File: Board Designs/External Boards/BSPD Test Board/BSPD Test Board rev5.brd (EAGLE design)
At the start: 64 x 85.8 mm, 30 parts

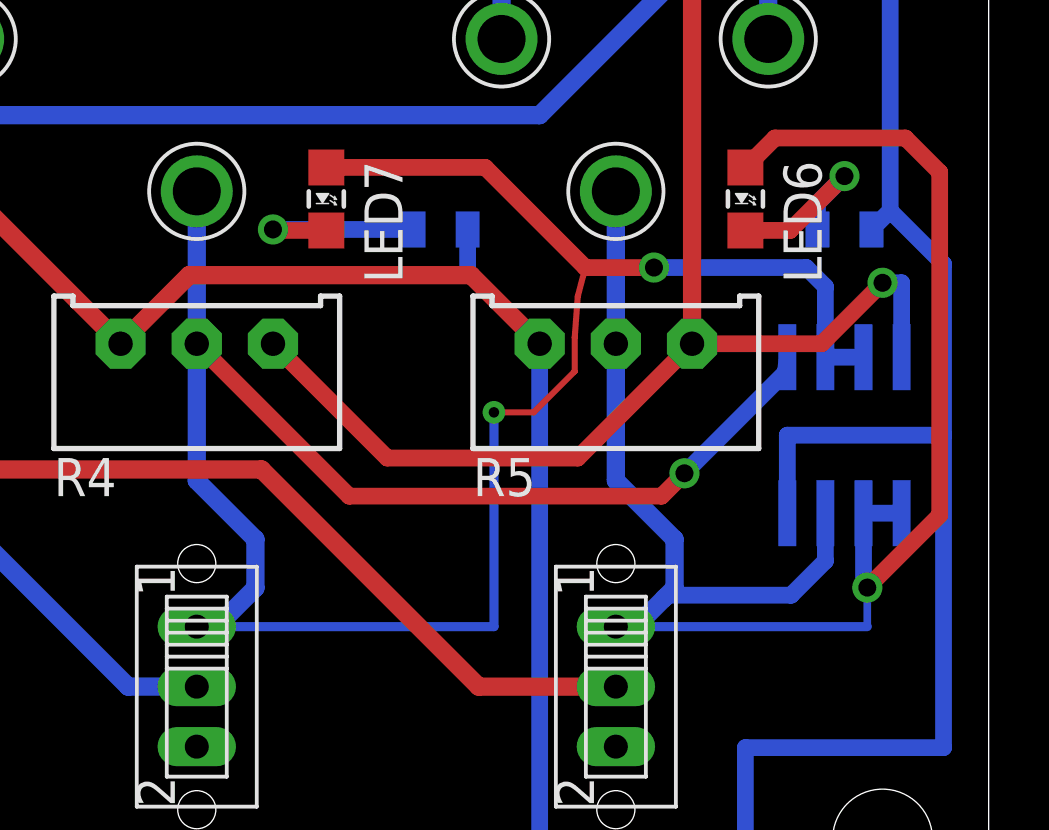
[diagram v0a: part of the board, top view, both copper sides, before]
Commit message: Minor routing changes
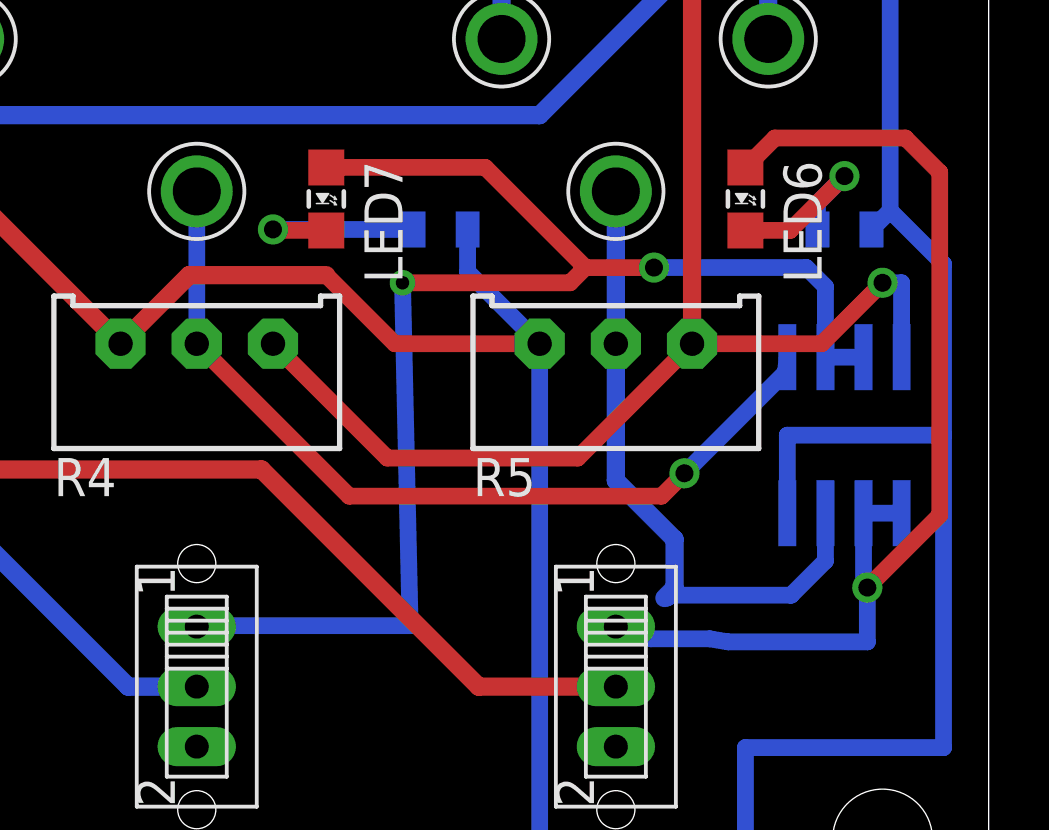
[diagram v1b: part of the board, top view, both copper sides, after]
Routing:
- net N$4: track 40.3 -> 29.0 mm, vias 2 -> 1
- net N$5: track 23.8 -> 22.0 mm
- net N$9: track 45.7 -> 46.8 mm
- net N$8: track 35.8 -> 36.3 mm
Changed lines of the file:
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@@
 </class>
 </classes>
-<designrules name="default">
+<designrules name="DRC Advanced Circuits">
 <description language="de">&lt;b&gt;EAGLE Design Rules&lt;/b&gt;
 &lt;p&gt;
@@
 <param name="mtCopper" value="0.035mm 0.035mm 0.035mm 0.035mm 0.035mm 0.035mm 0.035mm 0.035mm 0.035mm 0.035mm 0.035mm 0.035mm 0.035mm 0.035mm 0.035mm 0.035mm"/>
 <param name="mtIsolate" value="1.5mm 0.15mm 0.2mm 0.15mm 0.2mm 0.15mm 0.2mm 0.15mm 0.2mm 0.15mm 0.2mm 0.15mm 0.2mm 0.15mm 0.2mm"/>
-<param name="mdWireWire" value="8mil"/>
-<param name="mdWirePad" value="8mil"/>
-<param name="mdWireVia" value="8mil"/>
-<param name="mdPadPad" value="8mil"/>
-<param name="mdPadVia" value="8mil"/>
-<param name="mdViaVia" value="8mil"/>
-<param name="mdSmdPad" value="8mil"/>
-<param name="mdSmdVia" value="8mil"/>
-<param name="mdSmdSmd" value="8mil"/>
-<param name="mdViaViaSameLayer" value="8mil"/>
+<param name="mdWireWire" value="6mil"/>
+<param name="mdWirePad" value="6mil"/>
+<param name="mdWireVia" value="6mil"/>
+<param name="mdPadPad" value="6mil"/>
+<param name="mdPadVia" value="6mil"/>
+<param name="mdViaVia" value="6mil"/>
+<param name="mdSmdPad" value="6mil"/>
+<param name="mdSmdVia" value="6mil"/>
+<param name="mdSmdSmd" value="6mil"/>
+<param name="mdViaViaSameLayer" value="6mil"/>
 <param name="mnLayersViaInSmd" value="2"/>
 <param name="mdCopperDimension" value="40mil"/>
-<param name="mdDrill" value="8mil"/>
+<param name="mdDrill" value="6mil"/>
 <param name="mdSmdStop" value="0mil"/>
-<param name="msWidth" value="10mil"/>
-<param name="msDrill" value="24mil"/>
+<param name="msWidth" value="6mil"/>
+<param name="msDrill" value="15mil"/>
 <param name="msMicroVia" value="9.99mm"/>
 <param name="msBlindViaRatio" value="0.5"/>
@@
 <wire x1="23.368" y1="63.754" x2="20.422" y2="63.754" width="0.6096" layer="16"/>
 <wire x1="35.052" y1="20.32" x2="37.338" y2="22.606" width="0.6096" layer="1"/>
-<wire x1="46.736" y1="22.606" x2="49.022" y2="20.32" width="0.6096" layer="1"/>
-<wire x1="37.338" y1="22.606" x2="46.736" y2="22.606" width="0.6096" layer="1"/>
+<wire x1="41.91" y1="22.606" x2="37.338" y2="22.606" width="0.6096" layer="1"/>
 <contactref element="U$7" pad="4"/>
 <contactref element="R9" pad="2"/>
@@
 <wire x1="2.794" y1="22.86" x2="5.886" y2="22.86" width="0.5588" layer="16"/>
 <wire x1="49.022" y1="20.32" x2="49.022" y2="2.59926875" width="0.5588" layer="16"/>
-<wire x1="62.484" y1="6.5659" x2="62.484" y2="6.858" width="0" layer="19" extent="1-16"/>
 <wire x1="62.484" y1="6.858" x2="62.484" y2="17.272" width="0.5588" layer="16"/>
 <wire x1="49.022" y1="2.59926875" x2="55.88" y2="2.59926875" width="0.5588" layer="16"/>
 <wire x1="55.88" y1="2.59926875" x2="55.88" y2="6.858" width="0.5588" layer="16"/>
 <wire x1="55.88" y1="6.858" x2="62.484" y2="6.858" width="0.5588" layer="16"/>
+<wire x1="49.022" y1="20.32" x2="44.196" y2="20.32" width="0.5588" layer="1"/>
+<wire x1="44.196" y1="20.32" x2="41.91" y2="22.606" width="0.5588" layer="1"/>
 </signal>
 <signal name="N$1">
@@
 <contactref element="R4" pad="2"/>
 <contactref element="U$2" pad="P$1"/>
-<wire x1="37.592" y1="20.32" x2="37.592" y2="25.4" width="0.6096" layer="16"/>
-<wire x1="38.402125" y1="11.0363" x2="39.5478" y2="12.181975" width="0.6096" layer="16"/>
-<wire x1="39.5478" y1="12.181975" x2="39.5478" y2="13.802225" width="0.6096" layer="16"/>
-<wire x1="37.7383" y1="11.0363" x2="38.402125" y2="11.0363" width="0.6096" layer="16"/>
-<wire x1="37.592" y1="15.758025" x2="37.592" y2="20.32" width="0.6096" layer="16"/>
-<wire x1="39.5478" y1="13.802225" x2="37.592" y2="15.758025" width="0.6096" layer="16"/>
 <contactref element="U$7" pad="5"/>
 <wire x1="57.277" y1="19.872" x2="57.21" y2="19.364" width="0.5588" layer="16"/>
@@
 <wire x1="42.672" y1="15.24" x2="37.592" y2="20.32" width="0.5588" layer="1"/>
 <wire x1="53.086" y1="15.24" x2="42.672" y2="15.24" width="0.5588" layer="1"/>
-<via x="37.592" y="25.4" extent="1-16" drill="0.35"/>
+<wire x1="37.592" y1="25.4" x2="37.592" y2="20.32" width="0.5588" layer="16"/>
 </signal>
 <signal name="N$5">
@@
 <contactref element="U$3" pad="P$1"/>
 <wire x1="51.562" y1="20.32" x2="51.562" y2="25.4" width="0.6096" layer="16"/>
-<wire x1="53.1799125" y1="11.8440875" x2="52.372125" y2="11.0363" width="0.6096" layer="16"/>
 <wire x1="53.1799125" y1="11.8440875" x2="53.5178" y2="12.181975" width="0.6096" layer="16"/>
 <wire x1="53.5178" y1="12.181975" x2="53.5178" y2="13.802225" width="0.6096" layer="16"/>
-<wire x1="51.7083" y1="11.0363" x2="52.372125" y2="11.0363" width="0.6096" layer="16"/>
 <wire x1="51.562" y1="15.758025" x2="51.562" y2="20.32" width="0.6096" layer="16"/>
 <wire x1="53.5178" y1="13.802225" x2="51.562" y2="15.758025" width="0.6096" layer="16"/>
@@
 <wire x1="58.547" y1="13.081" x2="57.404" y2="11.938" width="0.5588" layer="16"/>
 <wire x1="57.404" y1="11.938" x2="53.273825" y2="11.938" width="0.5588" layer="16"/>
-<wire x1="53.273825" y1="11.938" x2="53.1799125" y2="11.8440875" width="0.5588" layer="16"/>
+<wire x1="53.273825" y1="11.938" x2="53.273825" y2="11.8440875" width="0.5588" layer="16"/>
+<wire x1="53.273825" y1="11.8440875" x2="53.1799125" y2="11.8440875" width="0.5588" layer="16"/>
 </signal>
 <signal name="N$6">
@@
 <wire x1="59.944" y1="12.192" x2="62.357" y2="14.605" width="0.5588" layer="1"/>
 <contactref element="SW_INT_BR" pad="P$1"/>
-<wire x1="51.562" y1="10.89" x2="59.944" y2="10.89" width="0.3048" layer="16"/>
-<wire x1="59.944" y1="10.89" x2="59.944" y2="12.192" width="0.254" layer="16"/>
+<wire x1="59.944" y1="12.192" x2="59.944" y2="10.382" width="0.5588" layer="16"/>
+<wire x1="55.30755625" y1="10.382" x2="59.944" y2="10.382" width="0.5588" layer="16"/>
+<wire x1="55.30755625" y1="10.382" x2="54.69775625" y2="10.4838" width="0.5588" layer="16"/>
+<wire x1="54.69775625" y1="10.4838" x2="52.7302" y2="10.4838" width="0.5588" layer="16"/>
+<wire x1="52.7302" y1="10.4838" x2="51.562" y2="10.89" width="0.5588" layer="16"/>
 </signal>
 <signal name="N$9">
@@
 <wire x1="57.912" y1="22.86" x2="58.547" y2="22.225" width="0.5588" layer="16"/>
 <contactref element="SW_INT_CUR" pad="P$1"/>
-<wire x1="47.498" y1="10.89" x2="37.592" y2="10.89" width="0.3048" layer="16"/>
-<wire x1="50.546" y1="22.86" x2="50.292" y2="21.90053125" width="0.2032" layer="1"/>
-<wire x1="50.292" y1="21.90053125" x2="50.1904" y2="20.52893125" width="0.2032" layer="1"/>
-<wire x1="48.82453125" y1="18.034" x2="47.498" y2="18.034" width="0.2032" layer="1"/>
-<wire x1="50.1904" y1="19.39986875" x2="48.82453125" y2="18.034" width="0.2032" layer="1"/>
-<wire x1="50.1904" y1="20.52893125" x2="50.1904" y2="19.39986875" width="0.2032" layer="1"/>
-<via x="47.498" y="18.034" extent="1-16" drill="0.35"/>
-<wire x1="47.498" y1="10.89" x2="47.498" y2="18.034" width="0.3048" layer="16"/>
+<wire x1="50.546" y1="22.86" x2="50.038" y2="22.352" width="0.5588" layer="1"/>
+<wire x1="50.038" y1="22.352" x2="44.45" y2="22.352" width="0.5588" layer="1"/>
+<via x="44.45" y="22.352" extent="1-16" drill="0.45"/>
+<wire x1="44.45" y1="22.352" x2="44.704" y2="10.922" width="0.5588" layer="16"/>
+<wire x1="44.704" y1="10.922" x2="41.402" y2="10.922" width="0" layer="19" extent="1-16"/>
+<wire x1="41.402" y1="10.922" x2="41.402" y2="10.668" width="0" layer="19" extent="1-16"/>
+<wire x1="44.704" y1="10.922" x2="37.846" y2="10.922" width="0.5588" layer="16"/>
+<wire x1="37.846" y1="10.922" x2="37.592" y2="10.89" width="0.5588" layer="16"/>
 </signal>
 <signal name="N$10">
